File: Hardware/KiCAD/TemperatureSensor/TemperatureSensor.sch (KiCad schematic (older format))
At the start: 1 part

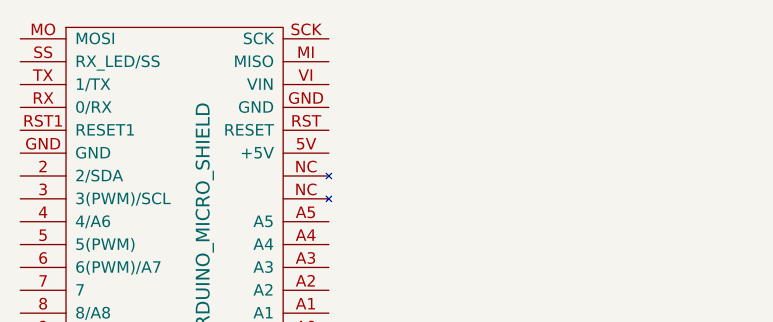
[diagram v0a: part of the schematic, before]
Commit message: working on temp sensors
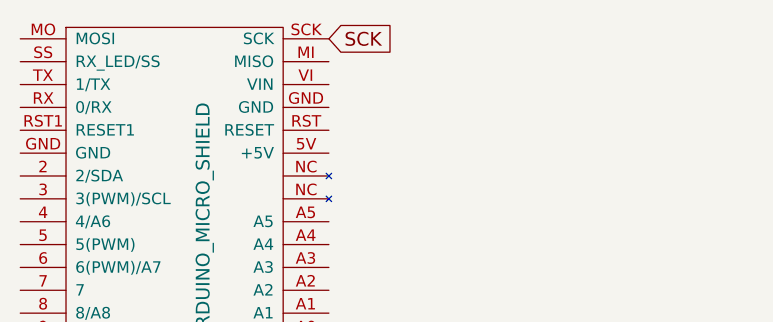
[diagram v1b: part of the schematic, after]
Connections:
- net SCK: now reaches U?.SCK
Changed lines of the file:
@@
 	0    1    1    0
 $EndComp
+Text GLabel 3000 2050 2    60   Input ~ 0
+SCK
 $EndSCHEMATC

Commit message: latest cs bug fixes and kicad
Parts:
- gave numbers to parts that had none: 1
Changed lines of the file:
@@
 $EndSheet
 $Comp
-L ARDUINO_MICRO_SHIELD U?
+L ARDUINO_MICRO_SHIELD U1
 U 1 1 5A00EB35
 P 1850 2000
-F 0 "U?" H 3600 2400 60  0000 C CNN
+F 0 "U1" H 3600 2400 60  0000 C CNN
 F 1 "ARDUINO_MICRO_SHIELD" H 2700 2600 60  0000 C CNN
 F 2 "" H 2250 1950 60  0000 C CNN

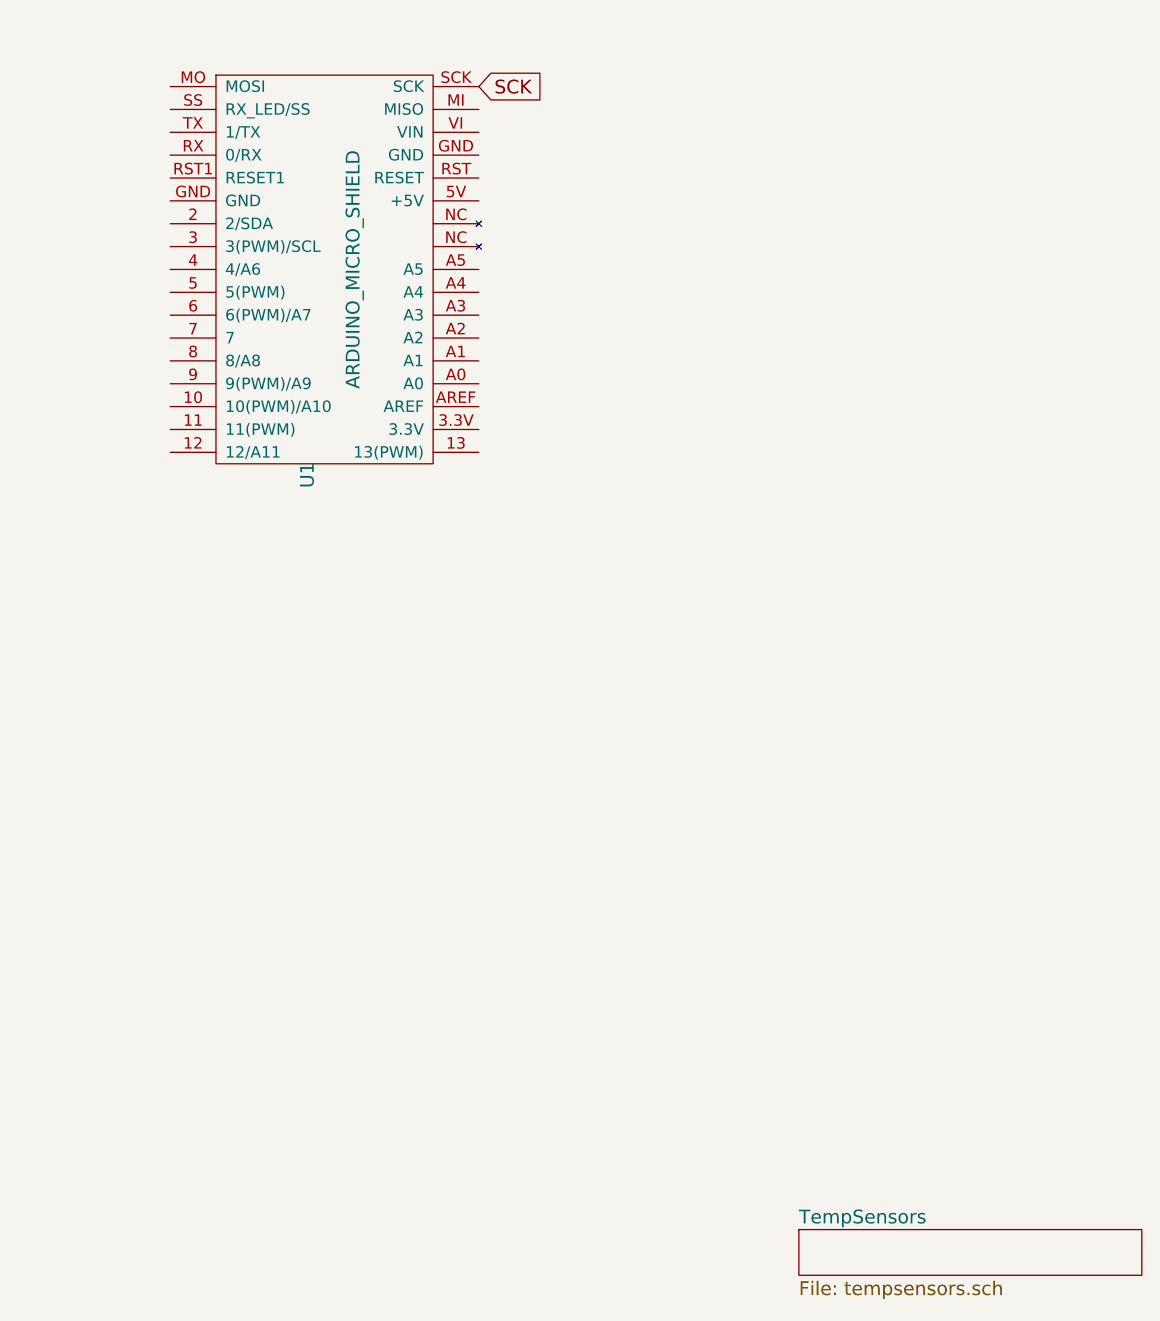
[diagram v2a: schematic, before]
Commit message: working on temp sensors
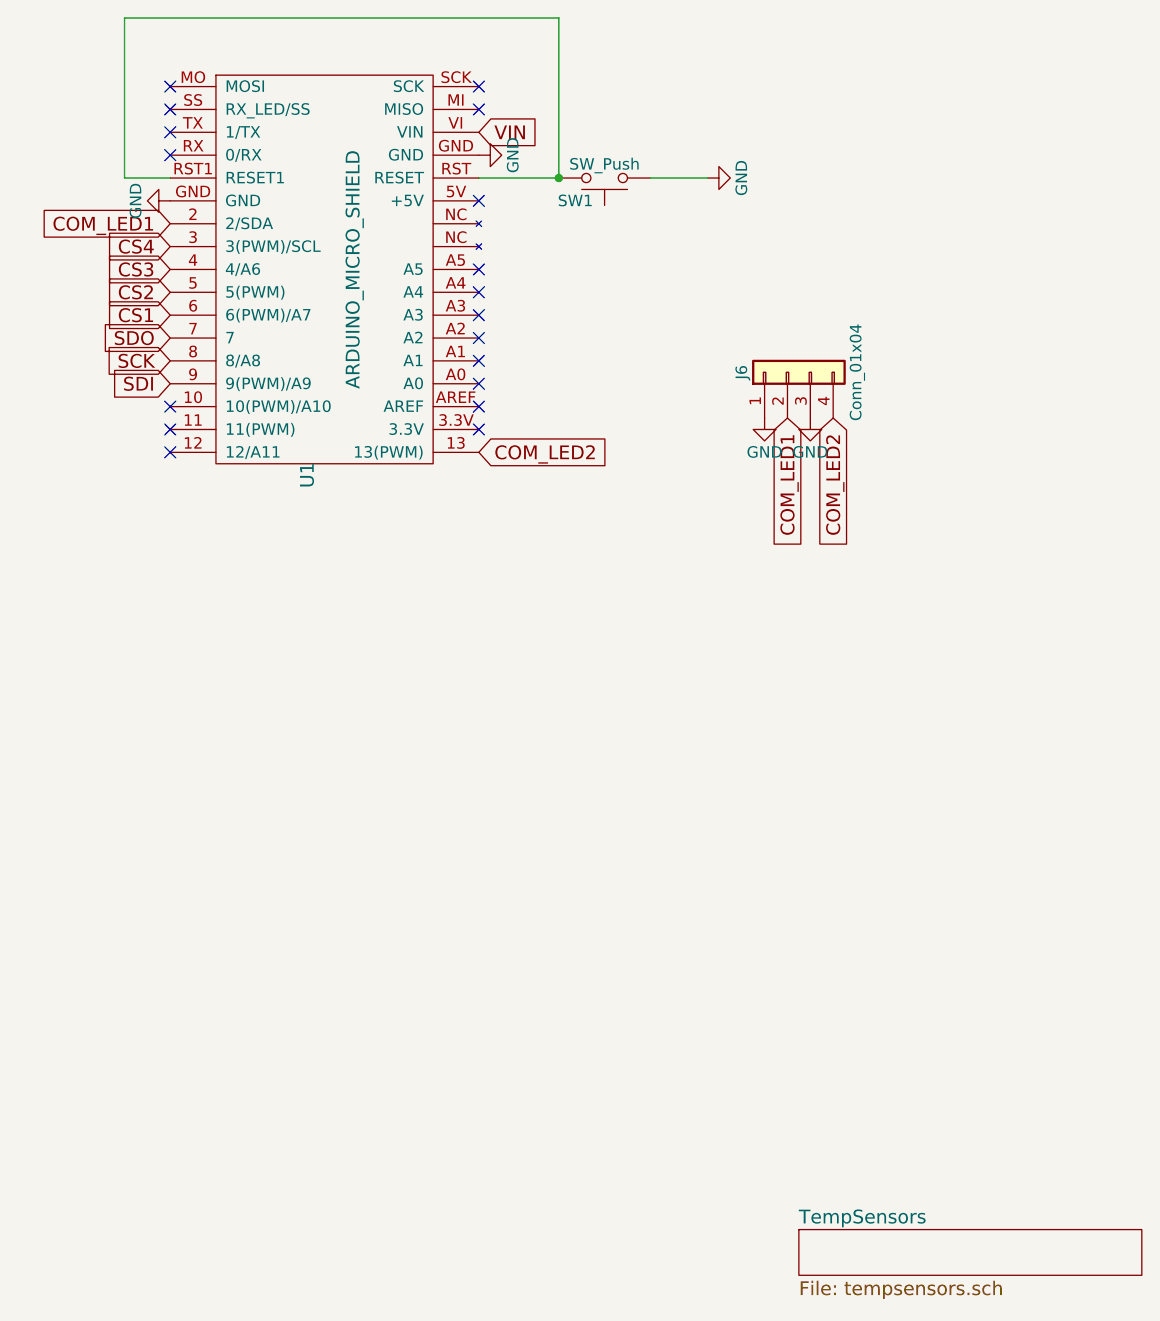
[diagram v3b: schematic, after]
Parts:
- added J6: Conn_01x04, TerminalBlocks_Phoenix:TerminalBlock_Phoenix_MPT-2.54mm_4pol, symbol Conn_01x04
- added SW1: SW_Push, Buttons_Switches_THT:SW_Tactile_SPST_Angled_PTS645Vx39-2LFS, symbol SW_Push
- U1: footprint (none) -> TemperatureSensor:ARDUINO_MICRO_SHIELD
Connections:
- net SCK: now also U1.8 (8/A8); no longer U1.SCK
- net COM_LED2: now reaches U1.13 (13(PWM))
- net COM_LED2: now also J6.4 (Pin_4)
- net COM_LED1: now reaches U1.2 (2/SDA)
- net COM_LED1: now also J6.2 (Pin_2)
- net CS4: now reaches U1.3 (3(PWM)/SCL)
- net CS3: now reaches U1.4 (4/A6)
- net CS2: now reaches U1.5 (5(PWM))
- net CS1: now reaches U1.6 (6(PWM)/A7)
- net SDO: now reaches U1.7
- net SDI: now reaches U1.9 (9(PWM)/A9)
- net GND: now reaches U1.GND
- net GND: now also J6.1 (Pin_1), J6.3 (Pin_3), SW1.1
- net at U1.RST (RESET): now also U1.RST1 (RESET1), SW1.2
- net VIN: now reaches U1.VI (VIN)
- no-connect marks 0 -> 18
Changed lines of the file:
@@
 F 0 "U1" H 3600 2400 60  0000 C CNN
 F 1 "ARDUINO_MICRO_SHIELD" H 2700 2600 60  0000 C CNN
-F 2 "" H 2250 1950 60  0000 C CNN
+F 2 "TemperatureSensor:ARDUINO_MICRO_SHIELD" H 2250 1950 60  0001 C CNN
 F 3 "" H 2250 1950 60  0000 C CNN
 	1    1850 2000
 	0    1    1    0
 $EndComp
-Text GLabel 3000 2050 2    60   Input ~ 0
+Text GLabel 1650 3250 0    60   Input ~ 0
 SCK
+Text GLabel 1650 3150 0    60   Input ~ 0
+SDO
+Text GLabel 1650 3350 0    60   Input ~ 0
+SDI
+$Comp
+L GND #PWR01
+U 1 1 5A134B36
+P 1650 2550
+F 0 "#PWR01" H 1650 2300 50  0001 C CNN
+F 1 "GND" H 1650 2400 50  0000 C CNN
+F 2 "" H 1650 2550 50  0001 C CNN
+F 3 "" H 1650 2550 50  0001 C CNN
+	1    1650 2550
+	0    1    1    0
+$EndComp
+$Comp
+L GND #PWR02
+U 1 1 5A134B61
+P 3000 2350
+F 0 "#PWR02" H 3000 2100 50  0001 C CNN
+F 1 "GND" H 3000 2200 50  0000 C CNN
+F 2 "" H 3000 2350 50  0001 C CNN
+F 3 "" H 3000 2350 50  0001 C CNN
+	1    3000 2350
+	0    -1   -1   0
+$EndComp
+Text GLabel 1650 3050 0    60   Input ~ 0
+CS1
+Text GLabel 1650 2950 0    60   Input ~ 0
+CS2
+Text GLabel 1650 2850 0    60   Input ~ 0
+CS3
+Text GLabel 1650 2750 0    60   Input ~ 0
+CS4
+NoConn ~ 3000 2850
+NoConn ~ 3000 2950
+NoConn ~ 3000 3050
+NoConn ~ 3000 3150
+NoConn ~ 3000 3250
+NoConn ~ 3000 3350
+NoConn ~ 3000 3450
+NoConn ~ 1650 2150
+NoConn ~ 1650 2250
+NoConn ~ 1650 2350
+NoConn ~ 1650 3450
+NoConn ~ 1650 3550
+NoConn ~ 1650 3650
+NoConn ~ 3000 2050
+NoConn ~ 1650 2050
+NoConn ~ 3000 2150
+$Comp
+L SW_Push SW1
+U 1 1 5A20263C
+P 3550 2450
+F 0 "SW1" H 3600 2550 50  0000 L CNN
+F 1 "SW_Push" H 3550 2390 50  0000 C CNN
+F 2 "Buttons_Switches_THT:SW_Tactile_SPST_Angled_PTS645Vx39-2LFS" H 3550 2650 50  0001 C CNN
+F 3 "" H 3550 2650 50  0001 C CNN
+	1    3550 2450
+	-1   0    0    1
+$EndComp
+$Comp
+L GND #PWR03
+U 1 1 5A202846
+P 4000 2450
+F 0 "#PWR03" H 4000 2200 50  0001 C CNN
+F 1 "GND" H 4000 2300 50  0000 C CNN
+F 2 "" H 4000 2450 50  0001 C CNN
+F 3 "" H 4000 2450 50  0001 C CNN
+	1    4000 2450
+	0    -1   1    0
+$EndComp
+Text GLabel 3000 2250 2    60   Input ~ 0
+VIN
+NoConn ~ 3000 3550
+NoConn ~ 3000 2550
+Wire Wire Line
+	3000 2450 3350 2450
+Wire Wire Line
+	3750 2450 4000 2450
+Wire Wire Line
+	1650 2450 1450 2450
+Wire Wire Line
+	1450 2450 1450 1750
+Wire Wire Line
+	1450 1750 3350 1750
+Wire Wire Line
+	3350 1750 3350 2450
+Connection ~ 3350 2450
+$Comp
+L Conn_01x04 J6
+U 1 1 5A26C022
+P 4350 3300
+F 0 "J6" H 4350 3500 50  0000 C CNN
+F 1 "Conn_01x04" H 4350 3000 50  0000 C CNN
+F 2 "TerminalBlocks_Phoenix:TerminalBlock_Phoenix_MPT-2.54mm_4pol" H 4350 3300 50  0001 C CNN
+F 3 "" H 4350 3300 50  0001 C CNN
+	1    4350 3300
+	0    -1   -1   0
+$EndComp
+Text GLabel 1650 2650 0    60   Input ~ 0
+COM_LED1
+Text GLabel 3000 3650 2    60   Input ~ 0
+COM_LED2
+Text GLabel 4550 3500 3    60   Input ~ 0
+COM_LED2
+Text GLabel 4350 3500 3    60   Input ~ 0
+COM_LED1
+$Comp
+L GND #PWR04
+U 1 1 5A26C0A6
+P 4250 3500
+F 0 "#PWR04" H 4250 3250 50  0001 C CNN
+F 1 "GND" H 4250 3350 50  0000 C CNN
+F 2 "" H 4250 3500 50  0001 C CNN
+F 3 "" H 4250 3500 50  0001 C CNN
+	1    4250 3500
+	-1   0    0    -1
+$EndComp
+$Comp
+L GND #PWR05
+U 1 1 5A26C0BA
+P 4450 3500
+F 0 "#PWR05" H 4450 3250 50  0001 C CNN
+F 1 "GND" H 4450 3350 50  0000 C CNN
+F 2 "" H 4450 3500 50  0001 C CNN
+F 3 "" H 4450 3500 50  0001 C CNN
+	1    4450 3500
+	-1   0    0    -1
+$EndComp
 $EndSCHEMATC

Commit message: test ltest layouayout
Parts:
- U1: footprint TemperatureSensor:ARDUINO_MICRO_SHIELD -> TemperatureSensor:ARDUINO_MICRO_SHIELD1
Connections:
- net at SW1.2, U1.RST (RESET): no longer U1.RST1 (RESET1)
- no-connect marks 18 -> 21
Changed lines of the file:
@@
 F 0 "U1" H 3600 2400 60  0000 C CNN
 F 1 "ARDUINO_MICRO_SHIELD" H 2700 2600 60  0000 C CNN
-F 2 "TemperatureSensor:ARDUINO_MICRO_SHIELD" H 2250 1950 60  0001 C CNN
+F 2 "TemperatureSensor:ARDUINO_MICRO_SHIELD1" H 2250 1950 60  0001 C CNN
 F 3 "" H 2250 1950 60  0000 C CNN
 	1    1850 2000
@@
 NoConn ~ 3000 2550
 Wire Wire Line
-	3000 2450 3350 2450
-Wire Wire Line
 	3750 2450 4000 2450
-Wire Wire Line
-	1650 2450 1450 2450
-Wire Wire Line
-	1450 2450 1450 1750
-Wire Wire Line
-	1450 1750 3350 1750
-Wire Wire Line
-	3350 1750 3350 2450
-Connection ~ 3350 2450
 $Comp
 L Conn_01x04 J6
@@
 	-1   0    0    -1
 $EndComp
+NoConn ~ 3000 2650
+NoConn ~ 3000 2750
+NoConn ~ 1650 2450
+Wire Wire Line
+	3350 2450 3000 2450
 $EndSCHEMATC
